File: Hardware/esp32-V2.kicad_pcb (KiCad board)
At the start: 4 copper layers, 103.7 x 68 mm, 118 parts, among them J1 Conn_01x01_Socket, J10 USB_C_Receptacle_USB2.0_16P, J11 PM254-1-17-Z-8.5, J12 MSD-4-A, J13 Conn_01x08, J2 Conn_01x01_Socket, J3 ER-CON06HT-1, J5 ER-CON50HT-1, J7 Conn_01x01_Socket, J8 Conn_01x01_Socket, Q2 DMP3015LSS-13, SW1 SW_Push_DPDT, SW4 SW_Push, SW5 SW_Push, U1 ESP32-S31-WROOM-3-N16R16V, U2 TPS61170DRVR, U3 MAX17055ETB+T, U4 TPS61022, U5 LT1963AEST-3.3#TRPBF, U6 MT3608, U7 TPS63700, U8 CN3158

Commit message: Layout: unrouted = 0
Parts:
- added R14: 100k, Resistor_SMD:R_0402_1005Metric, F.Cu at (204.0, 69.5)
- J3: value ER-CON06HT-1 -> KH-FG0.5-H2.0-6PIN
- J5: value ER-CON50HT-1 -> HC-FPC-0.5-50P-FHH20
- NT1: footprint NetTie:NetTie-2_SMD_Pad0.5mm -> YV:NetTie-2_SMD_Pad0.16mm
- moved C25 90.4 mm to (130.2, 93.8)
- moved D15 65.2 mm to (159.4, 97.5), turned to -90 degrees
- moved L9 62.5 mm to (155.4, 102.8)
- moved R11 55.6 mm to (153.8, 66.1), turned to -90 degrees
- moved R10 54.3 mm to (153.8, 68.1), turned to 90 degrees
- moved C8 51.1 mm to (138.9, 103.0), turned to 90 degrees
- moved U3 50.4 mm to (136.5, 101.2), turned to 180 degrees
- moved C7 49.4 mm to (135.5, 103.8)
- moved R12 46.3 mm to (142.2, 89.0)
- moved NT1 44.3 mm to (134.2, 102.5)
- moved R9 43.1 mm to (131.8, 101.0), turned to 90 degrees
- moved D2 30.4 mm to (197.2, 65.5), turned to 90 degrees
- moved R13 27.2 mm to (152.7, 96.5), turned to -90 degrees
- moved D4 26.8 mm to (197.2, 63.5), turned to -90 degrees
- moved D14 23.9 mm to (205.5, 110.5), turned to -90 degrees
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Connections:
- D13 pad 2: /ESP32-S31/USB-Dp -> Net-(D13-A2)
- D14 pad 2: /ESP32-S31/USB-Dn -> Net-(D14-A2)
- J10 pad A6: Net-(J10-D+-PadA6) -> Net-(D13-A2)
- J10 pad A7: Net-(J10-D--PadA7) -> Net-(D14-A2)
- J10 pad B6: Net-(J10-D+-PadA6) -> Net-(D13-A2)
- J10 pad B7: Net-(J10-D--PadA7) -> Net-(D14-A2)
- J5 pad 0: unconnected-(J5-MountPin-PadMP) -> (no net)
- J5 pad 12: /ESP32-S31/DS15 -> GND
- J5 pad 13: /ESP32-S31/DS14 -> GND
- J5 pad 21: /ESP32-S31/DS7 -> GND
- J5 pad 22: /ESP32-S31/DS6 -> GND
- J5 pad 23: /ESP32-S31/DS5 -> GND
- J5 pad 3: /ESP32-S31/DS23 -> GND
- J5 pad 4: /ESP32-S31/DS22 -> GND
- J5 pad 5: /ESP32-S31/DS21 -> GND
- R36 pad 2: Net-(D15-A) -> +14.5V
- R6 pad 1: Net-(J10-D--PadA7) -> Net-(D14-A2)
- R7 pad 1: Net-(J10-D+-PadA6) -> Net-(D13-A2)
- R8 pad 2: EN -> BOOT
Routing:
- net GND: track 51.2 -> 159.6 mm, vias 42 -> 127
- net /ESP32-S31/I2C1-SDA: track 0.00 -> 108.1 mm, vias 0 -> 3
- net /ESP32-S31/I2C1-SCL: track 0.00 -> 105.1 mm, vias 0 -> 3
- net /DC-DC/BACKLIGHTen: track 0.00 -> 81.6 mm, vias 0 -> 2
- net EN: track 0.00 -> 76.9 mm, vias 0 -> 1
- net IO57: track 0.00 -> 75.4 mm, vias 0 -> 1
- net Net-(U4-EN): track 1.98 -> 76.5 mm, vias 0 -> 1
- net IO56: track 0.00 -> 71.3 mm, vias 0 -> 1
- net Net-(D8-K): track 1.64 -> 71.6 mm, vias 1 -> 2
- net BOOT: track 0.00 -> 69.2 mm, vias 0 -> 1
- net IO55: track 0.00 -> 67.4 mm, vias 0 -> 1
- net Net-(D7-A): track 0.00 -> 66.2 mm, vias 0 -> 2
- net Net-(D7-K): track 1.64 -> 67.5 mm, vias 1 -> 2
- net IO54: track 0.00 -> 63.9 mm, vias 0 -> 1
- net /ESP32-S31/Touch-RST: track 0.00 -> 52.7 mm, vias 0 -> 1
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- added copper zone on F.Cu, net +14.5V
- added copper zone on F.Cu, net +3.3V
- added copper zone on F.Cu, net GND
- added copper zone on F.Cu, net GNDREF
- added copper zone on In2.Cu, net Net-(F3-Pad1)
- added copper zone on F.Cu, net Net-(J1-Pin_1)
- added copper zone on F.Cu, net Net-(J2-Pin_1)
- added copper zone on F.Cu, net V-USB
- added copper zone on F.Cu, net Vbatt
- removed copper zone on In2.Cu, net /USB and Cells/Vin
- removed copper zone on F.Cu, net Net-(D3-A)
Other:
- outline, holes or cut-outs redrawn
- board text added: "Chrg."
- board text added: "I37"
- board text added: "I58"
- board text added: "I59"
- board text added: "IO35"
- board text added: "IO43"
- board text added: "IO44"
- board text added: "IO45"
- board text added: "IO46"
- board text added: "IO47"
- board text added: "IO48"
- board text added: "IO54"
- board text added: "IO55"
- board text added: "IO56"
- board text added: "IO57"
- board text removed: "Charging"
- board text removed: "I34"
- board text removed: "I35"
- board text removed: "IO0"
- board text removed: "IO12"
- board text removed: "IO13"
- board text removed: "IO14"
- board text removed: "IO15"
- board text removed: "IO21"
- board text removed: "IO22"
- board text removed: "IO25"
- board text removed: "IO26"
- board text removed: "IO27"
- board text removed: "IO32"
- board text removed: "VBATT"

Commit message: Layout cleaned
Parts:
- added REF**: KiCad-Logo2_12mm_SilkScreen, Symbol:KiCad-Logo2_12mm_SilkScreen, B.Cu at (134.3, 68.3)
- moved F3 1.26 mm to (207.8, 102.1)
- moved C32 0.25 mm to (135.5, 104.0)
- moved NT1 0.25 mm to (134.2, 102.2)
- moved D15 0.15 mm to (187.5, 117.0)
- renumbered C28 to C1, C14 to C10, C1 to C11, C25 to C12, C12 to C14, C30 to C18, C33 to C19, C35 to C20, C34 to C21, C25 to C22, C18 to C23, C19 to C24, C20 to C25, C21 to C26, C22 to C27, C23 to C28, C9 to C29, C24 to C30, C8 to C31, C7 to C32, C32 to C33, C31 to C34, C29 to C6, C6 to C7, C27 to C8, C26 to C9, D11 to D1, D3 to D10, D15 to D11, D14 to D12, D7 to D14, D8 to D15, D10 to D2, D9 to D3, D12 to D4, D4 to D6, D1 to D7, D2 to D8, D6 to D9, F2 to F1, F1 to F2, J5 to J10, J13 to J3, J12 to J4, J11 to J5, J10 to J6, J3 to J9, L8 to L4, L9 to L8, Q2 to Q1, R11 to R1, R32 to R10, R12 to R11, R17 to R12, R18 to R13, R35 to R14, R19 to R15, R36 to R16, R5 to R17, R20 to R18, R13 to R19, R1 to R2, R26 to R20, R23 to R21, R21 to R23, R9 to R24, R30 to R25, R29 to R26, R28 to R27, R27 to R28, R31 to R29, R10 to R3, R8 to R30, R6 to R31, R7 to R32, R16 to R33, R2 to R4, R14 to R5, R3 to R6, R34 to R7, R33 to R8, R4 to R9, SW5 to SW2, SW4 to SW3, TP3 to TP1, TP4 to TP2, TP1 to TP3, U2 to U1, U4 to U2, U1 to U3, U5 to U4, U8 to U5, U7 to U6, U6 to U7, U3 to U8
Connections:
- net /ESP32-S31/USB-Dn renamed /ESP32-S31/USB_D-
- net /ESP32-S31/USB-Dp renamed /ESP32-S31/USB_D+
- net Net-(D13-A2) renamed /USB and Cells/D+
- net Net-(D14-A2) renamed /USB and Cells/D-
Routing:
- net /ESP32-S31/I2C1-SDA: track 108.1 -> 114.0 mm
- net /ESP32-S31/I2C1-SCL: track 105.1 -> 110.2 mm
- net /ESP32-S31/USB_D-: track 44.2 -> 48.2 mm
- net /ESP32-S31/USB_D+: track 44.4 -> 48.2 mm
- net GNDREF: track 8.26 -> 4.53 mm
- net /DC-DC/BACKLIGHTen: track 81.6 -> 78.1 mm
- net IO54: track 63.9 -> 60.6 mm
- net IO55: track 67.4 -> 64.7 mm
- net Vbatt: track 50.7 -> 48.2 mm
- net IO56: track 71.3 -> 69.5 mm
- net V-USB: track 22.5 -> 21.0 mm
- net /ESP32-S31/DS2: track 46.8 -> 45.3 mm
- net Net-(F3-Pad1): track 8.00 -> 9.47 mm
- net /ESP32-S31/Touch-INT: track 51.4 -> 50.0 mm
- net IO57: track 75.4 -> 74.2 mm
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- added copper zone on B.Cu, net GND
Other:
- outline, holes or cut-outs redrawn
- board text added: "Designed by: Yannick Vallée, ing. 2026-10-08"
- board text removed: "Designed by: Yannick Vallée, ing. 2026-06-18"
- board text removed: "J5.12"
- board text removed: "JP1 X O JP2 O X JP3 X O"
- board text removed: "Vbatt ESP VN"

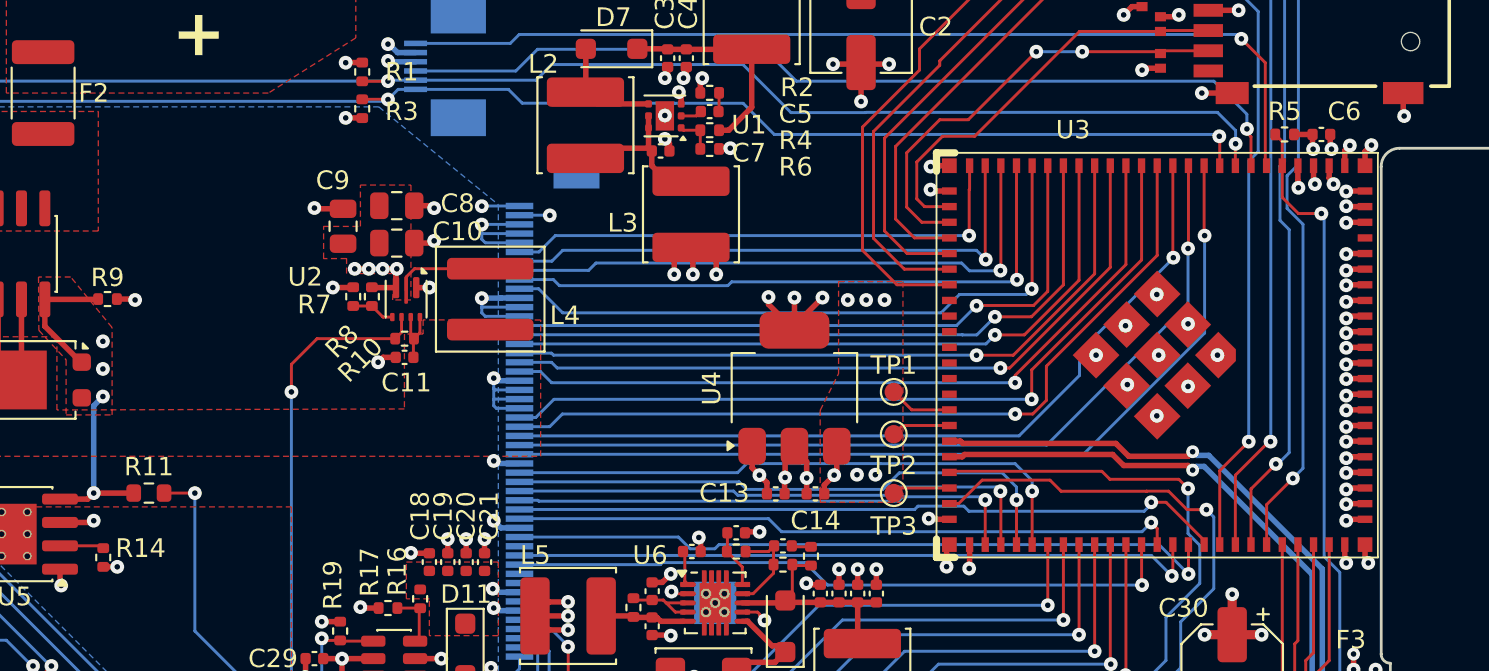
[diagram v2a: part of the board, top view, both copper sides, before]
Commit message: Update de la librairy et du BOM
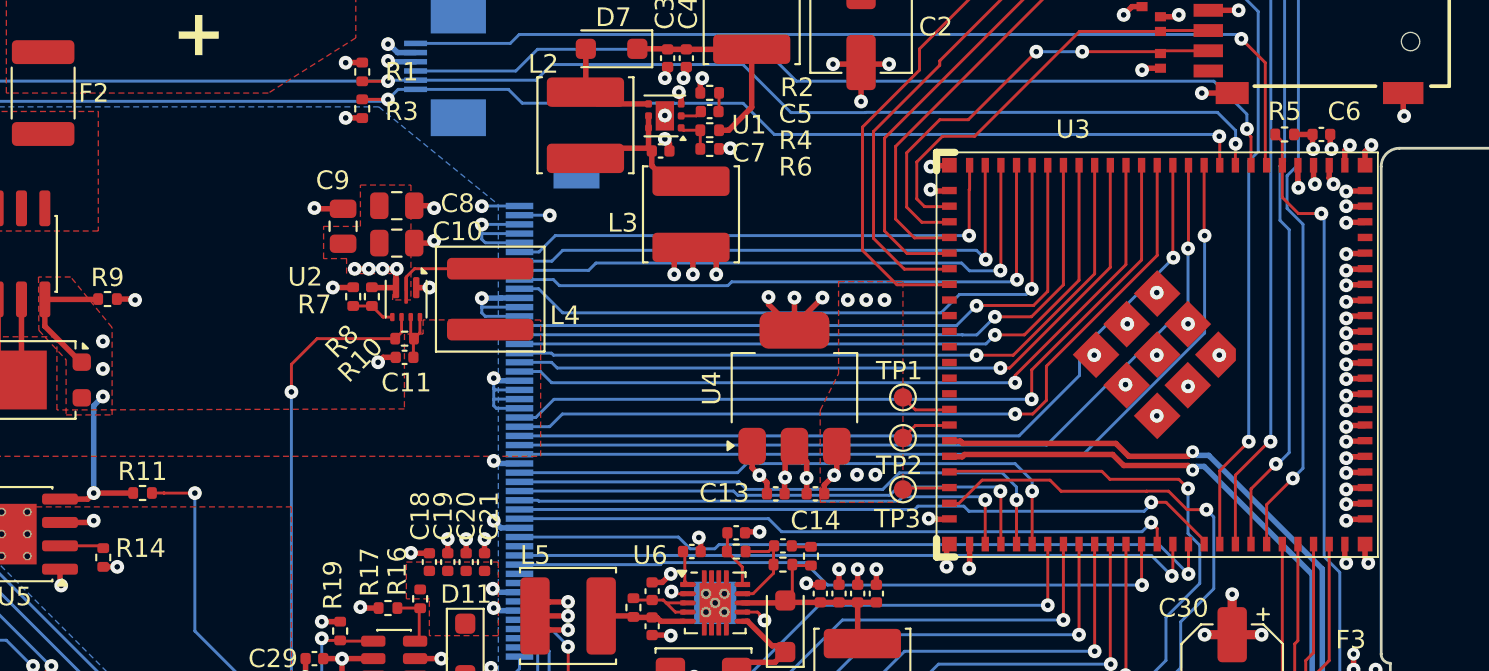
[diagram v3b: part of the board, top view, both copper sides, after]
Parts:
- D10, D11, D7: value D_Schottky -> Diode-DK24
- D9: value Fuxinsemi_PDS760 -> Diode-PDS760
- J3: value Conn_01x08 -> Conn_01x08_F_Header
- J6: value USB_C_Receptacle_USB2.0_16P -> USB_C_Receptacle-16p
- R11: footprint Resistor_SMD:R_0603_1608Metric -> Resistor_SMD:R_0402_1005Metric
- SW2, SW3: value SW_Push -> SW-000001
- U2: value TPS61022 -> IC-TPS61022
- U3: footprint PCM_Espressif:ESP32-S31-WROOM-3 -> YV:ESP32-S31-WROOM-3
- moved TP1 0.58 mm to (183.2, 83.8)
- moved TP2 0.54 mm to (183.2, 86.0)
- moved TP3 0.54 mm to (183.2, 88.8)
- moved R11 0.35 mm to (141.9, 89.0)
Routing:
- net Net-(D14-A): track 65.0 -> 65.7 mm
- net Net-(U3-USB_DP): track 3.43 -> 2.80 mm
- net Net-(U3-GPIO36*): track 3.14 -> 2.55 mm
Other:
- board text added: "Designed by: Yannick Vallée, ing. 2026-10-09"
- board text removed: "Designed by: Yannick Vallée, ing. 2026-10-08"
